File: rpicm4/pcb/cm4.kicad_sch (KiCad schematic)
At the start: 11 parts, among them J1 USB_C_Receptacle_USB2.0, J2 USB_C_Receptacle_USB2.0, J3 Conn_01x02_Male, J4 Conn_01x02_Male, J5 Conn_01x02_Male, J6 Conn_01x02_Male

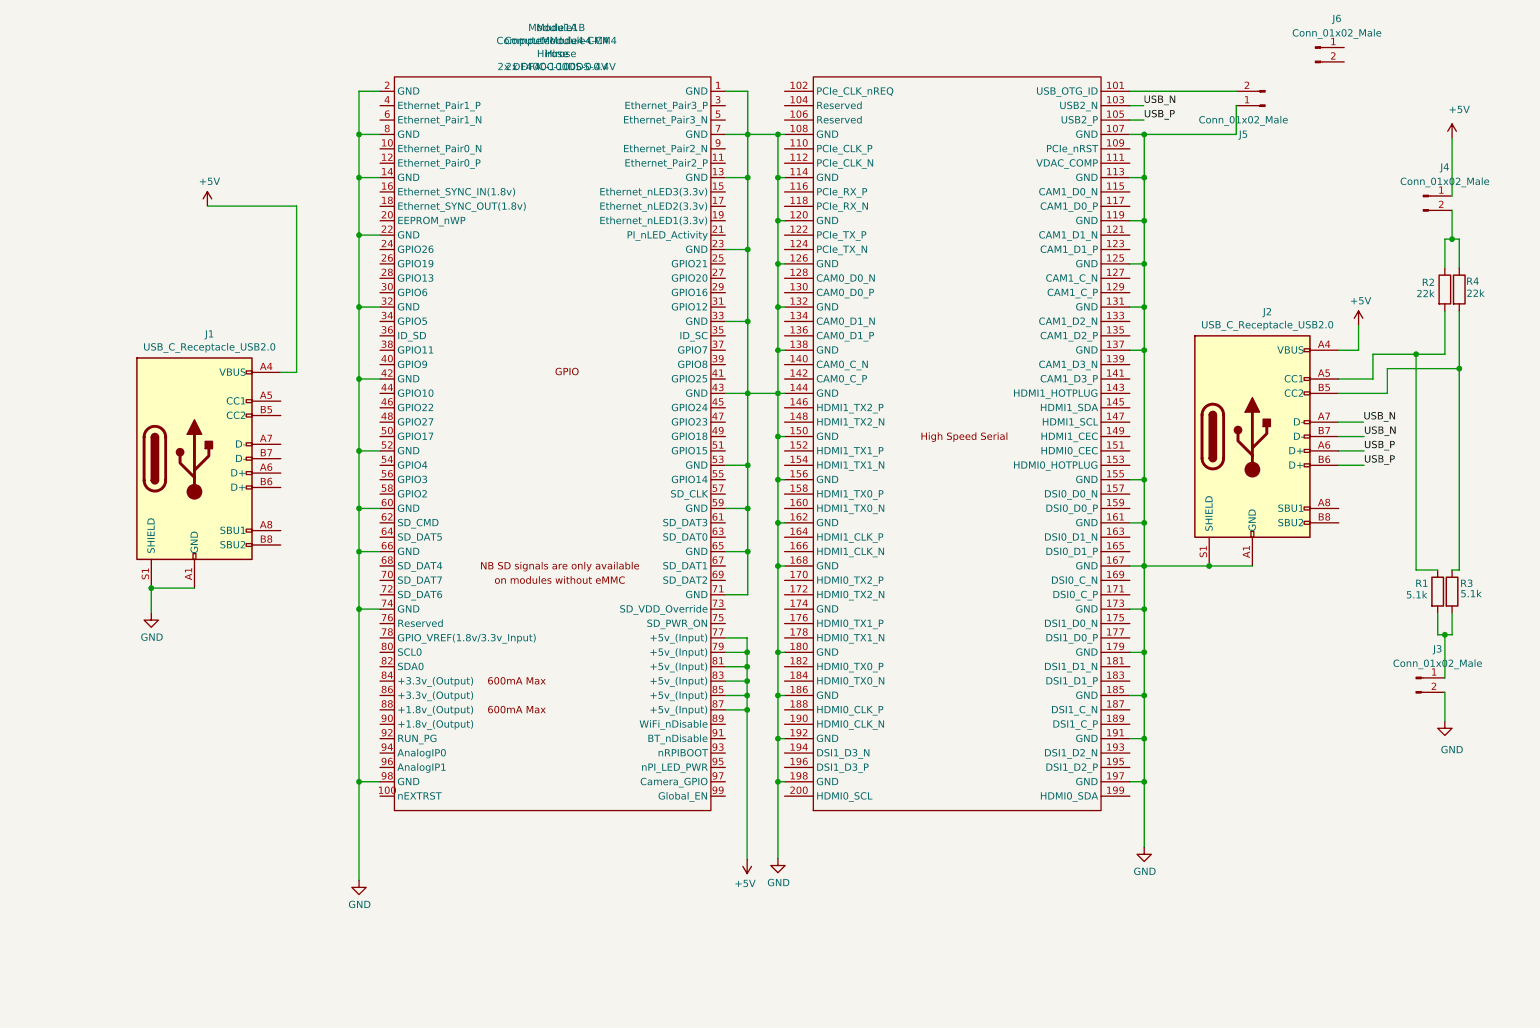
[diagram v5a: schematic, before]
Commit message: rpicm4: nRPIBOOT, UART, typec.cc
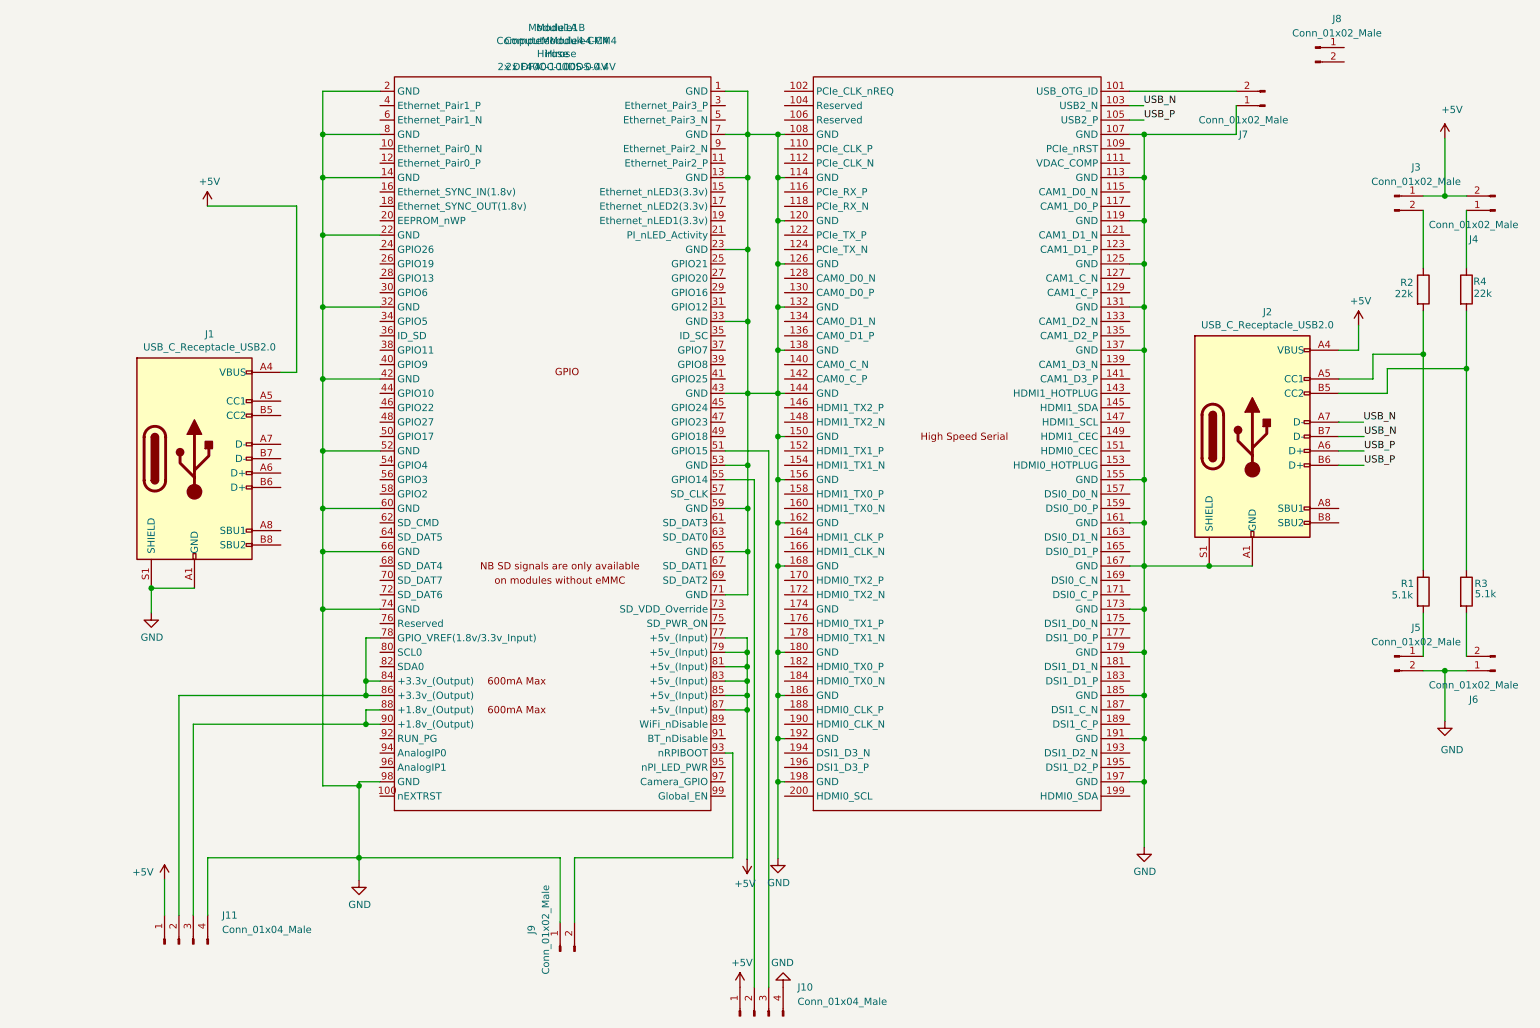
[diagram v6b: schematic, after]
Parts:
- added J10, J11: Conn_01x04_Male, Connector_PinHeader_2.54mm:PinHeader_1x04_P2.54mm_Vertical, symbol Connector:Conn_01x04_Male
- added J4, J6, J9: Conn_01x02_Male, Connector_PinHeader_2.54mm:PinHeader_1x02_P2.54mm_Vertical, symbol Connector:Conn_01x02_Male
- renumbered J4 to J3, J3 to J5, J5 to J7, J6 to J8
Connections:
- net +5V: now also J10.1 (Pin_1), J11.1 (Pin_1), J4.2 (Pin_2)
- net GND: now also J10.4 (Pin_4), J11.4 (Pin_4), J6.1 (Pin_1), J9.1 (Pin_1)
- net at J5.1 (Pin_1), R1.2: no longer R3.2
- net at J3.2 (Pin_2), R2.1: no longer R4.1
- net at Module1.51 (GPIO15): now also J10.3 (Pin_3)
- net at Module1.55 (GPIO14): now also J10.2 (Pin_2)
- net at Module1.78 (GPIO_VREF(1.8v/3.3v_Input)): now also Module1.84 (+3.3v_(Output)), Module1.86 (+3.3v_(Output)), J11.2 (Pin_2)
- net at Module1.88 (+1.8v_(Output)): now also Module1.90 (+1.8v_(Output)), J11.3 (Pin_3)
- net at Module1.93 (nRPIBOOT): now also J9.2 (Pin_2)
- new net: J6.2 (Pin_2), R3.2
- new net: J4.1 (Pin_1), R4.1
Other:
- moved on the sheet: J3, J5, R1, R2, R3, R4

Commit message: rpicm4: led pwr/act,analog 0/1,pwm 0/1,uart tx/rx
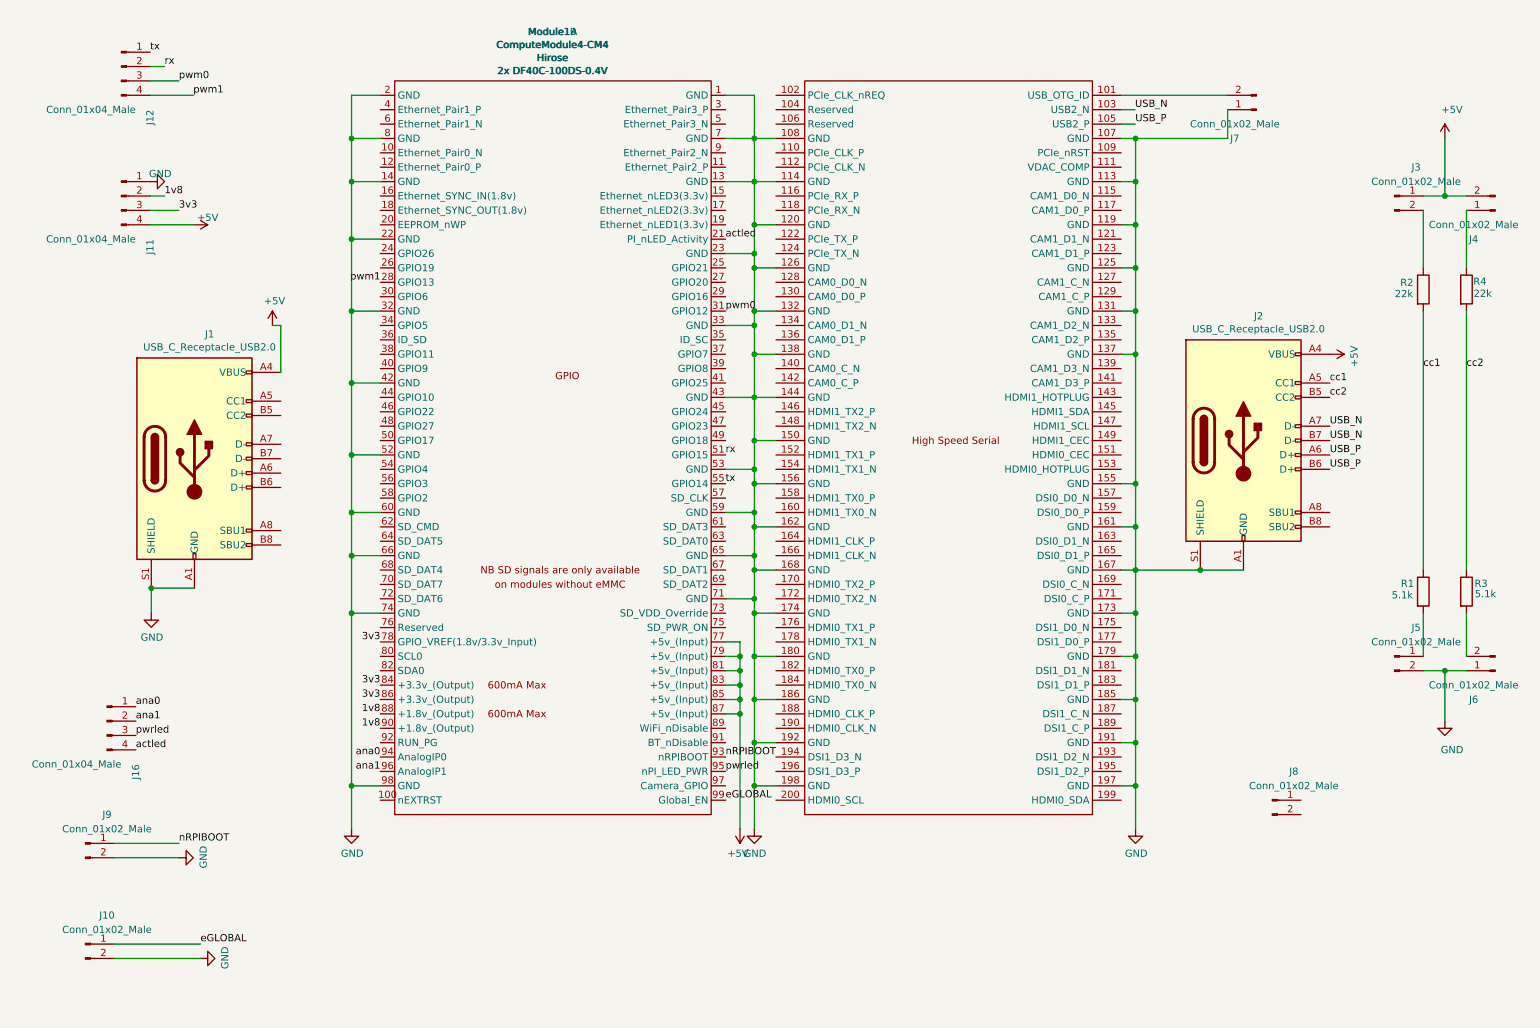
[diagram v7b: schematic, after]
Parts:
- removed J10: Conn_01x04_Male, Connector_PinHeader_2.54mm:PinHeader_1x04_P2.54mm_Vertical, symbol Connector:Conn_01x04_Male
- added J10: Conn_01x02_Male, Connector_PinHeader_2.54mm:PinHeader_1x02_P2.54mm_Vertical, symbol Connector:Conn_01x02_Male
- added J12, J16: Conn_01x04_Male, Connector_PinHeader_2.54mm:PinHeader_1x04_P2.54mm_Vertical, symbol Connector:Conn_01x04_Male
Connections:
- net +5V: now also J11.4 (Pin_4); no longer J11.1 (Pin_1)
- net GND: now also J11.1 (Pin_1), J9.2 (Pin_2), Module1.174 (GND), J10.2 (Pin_2); no longer J11.4 (Pin_4), J9.1 (Pin_1)
- net cc2: now reaches J2.B5 (CC2), R3.1, R4.2
- net cc1: now reaches J2.A5 (CC1), R1.1, R2.2
- net actled: now reaches Module1.21 (PI_nLED_Activity)
- net actled: now also J16.4 (Pin_4)
- net pwm1: now reaches Module1.28 (GPIO13)
- net pwm1: now also J12.4 (Pin_4)
- net pwm0: now reaches Module1.31 (GPIO12)
- net pwm0: now also J12.3 (Pin_3)
- net rx: now reaches Module1.51 (GPIO15)
- net rx: now also J12.2 (Pin_2)
- net tx: now reaches Module1.55 (GPIO14)
- net tx: now also J12.1 (Pin_1)
- net 3v3: now reaches Module1.78 (GPIO_VREF(1.8v/3.3v_Input)), Module1.84 (+3.3v_(Output)), Module1.86 (+3.3v_(Output))
- net 3v3: now also J11.3 (Pin_3); no longer J11.2 (Pin_2)
- net 1v8: now reaches Module1.88 (+1.8v_(Output)), Module1.90 (+1.8v_(Output))
- net 1v8: now also J11.2 (Pin_2); no longer J11.3 (Pin_3)
- net nRPIBOOT: now reaches Module1.93 (nRPIBOOT)
- net nRPIBOOT: now also J9.1 (Pin_1); no longer J9.2 (Pin_2)
- net ana0: now reaches Module1.94 (AnalogIP0)
- net ana0: now also J16.1 (Pin_1)
- net pwrled: now reaches Module1.95 (nPI_LED_PWR)
- net pwrled: now also J16.3 (Pin_3)
- net ana1: now reaches Module1.96 (AnalogIP1)
- net ana1: now also J16.2 (Pin_2)
- net eGLOBAL: now reaches Module1.99 (Global_EN)
- net eGLOBAL: now also J10.1 (Pin_1)
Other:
- moved on the sheet: J2, J7, J8, Module1A, Module1B

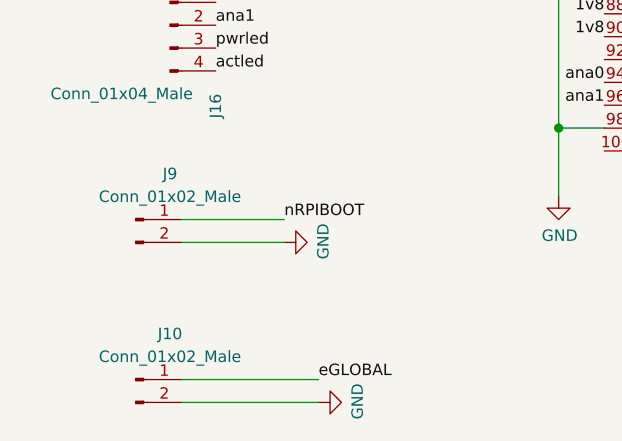
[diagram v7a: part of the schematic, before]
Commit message: rpicm4: round corner, better layout
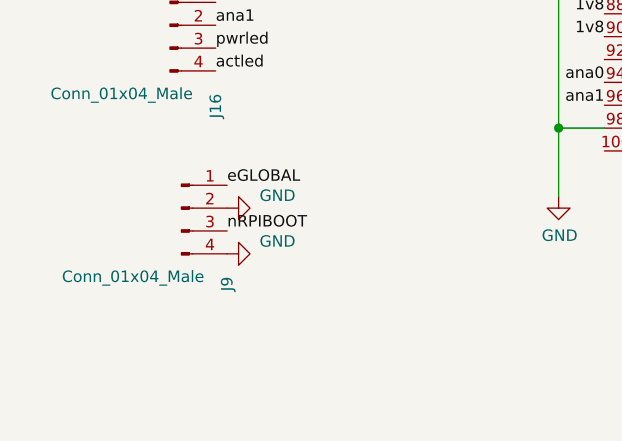
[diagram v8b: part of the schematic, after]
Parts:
- removed J10, J9: Conn_01x02_Male, Connector_PinHeader_2.54mm:PinHeader_1x02_P2.54mm_Vertical, symbol Connector:Conn_01x02_Male
- added J9: Conn_01x04_Male, Connector_PinHeader_2.54mm:PinHeader_1x04_P2.54mm_Vertical, symbol Connector:Conn_01x04_Male
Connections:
- net GND: now also J9.2 (Pin_2), J9.4 (Pin_4)
- net eGLOBAL: now also J9.1 (Pin_1)
- net nRPIBOOT: now also J9.3 (Pin_3)
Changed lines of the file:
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@@
   (junction (at 265.43 46.99) (diameter 1.016) (color 0 0 0 0))
   (junction (at 265.43 130.81) (diameter 1.016) (color 0 0 0 0))
-  (wire (pts (xy 30.48 161.29) (xy 41.91 161.29))
-    (stroke (width 0) (type solid) (color 0 0 0 0))
-  )
-  (wire (pts (xy 30.48 179.07) (xy 45.72 179.07))
-    (stroke (width 0) (type solid) (color 0 0 0 0))
-  )
   (wire (pts (xy 36.83 46.99) (xy 39.37 46.99))
     (stroke (width 0) (type solid) (color 0 0 0 0))
@@
     (stroke (width 0) (type solid) (color 0 0 0 0))
   )
-  (wire (pts (xy 41.91 163.83) (xy 30.48 163.83))
-    (stroke (width 0) (type solid) (color 0 0 0 0))
-  )
   (wire (pts (xy 44.45 29.21) (xy 36.83 29.21))
     (stroke (width 0) (type solid) (color 0 0 0 0))
   )
-  (wire (pts (xy 45.72 181.61) (xy 30.48 181.61))
-    (stroke (width 0) (type solid) (color 0 0 0 0))
-  )
   (wire (pts (xy 58.42 69.85) (xy 59.8932 69.85))
     (stroke (width 0) (type solid) (color 0 0 0 0))
@@
     (effects (font (size 1.27 1.27)) (justify left bottom))
   )
+  (label "eGLOBAL" (at 35.56 157.48 0)
+    (effects (font (size 1.27 1.27)) (justify left bottom))
+  )
+  (label "nRPIBOOT" (at 35.56 162.56 0)
+    (effects (font (size 1.27 1.27)) (justify left bottom))
+  )
   (label "tx" (at 36.83 21.59 0)
     (effects (font (size 1.27 1.27)) (justify left bottom))
@@
     (effects (font (size 1.27 1.27)) (justify left bottom))
   )
-  (label "nRPIBOOT" (at 41.91 161.29 0)
-    (effects (font (size 1.27 1.27)) (justify left bottom))
-  )
   (label "pwm1" (at 44.45 29.21 0)
-    (effects (font (size 1.27 1.27)) (justify left bottom))
-  )
-  (label "eGLOBAL" (at 45.72 179.07 0)
     (effects (font (size 1.27 1.27)) (justify left bottom))
   )
@@
     )
   )
+  (symbol (lib_id "power:GND") (at 35.56 160.02 90) (unit 1)
+    (in_bom yes) (on_board yes)
+    (property "Reference" "#PWR010" (id 0) (at 41.91 160.02 0)
+      (effects (font (size 1.27 1.27)) hide)
+    )
+    (property "Value" "GND" (id 1) (at 41.1544 158.6357 90))
+    (property "Footprint" "" (id 2) (at 35.56 160.02 0)
+      (effects (font (size 1.27 1.27)) hide)
+    )
+    (property "Datasheet" "" (id 3) (at 35.56 160.02 0)
+      (effects (font (size 1.27 1.27)) hide)
+    )
+  )
+  (symbol (lib_id "power:GND") (at 35.56 165.1 90) (unit 1)
+    (in_bom yes) (on_board yes)
+    (property "Reference" "#PWR012" (id 0) (at 41.91 165.1 0)
+      (effects (font (size 1.27 1.27)) hide)
+    )
+    (property "Value" "GND" (id 1) (at 41.1544 163.7157 90))
+    (property "Footprint" "" (id 2) (at 35.56 165.1 0)
+      (effects (font (size 1.27 1.27)) hide)
+    )
+    (property "Datasheet" "" (id 3) (at 35.56 165.1 0)
+      (effects (font (size 1.27 1.27)) hide)
+    )
+  )
   (symbol (lib_id "power:GND") (at 36.83 44.45 90) (unit 1)
     (in_bom yes) (on_board yes)
@@
     )
   )
-  (symbol (lib_id "power:GND") (at 41.91 163.83 90) (unit 1)
-    (in_bom yes) (on_board yes)
-    (property "Reference" "#PWR010" (id 0) (at 48.26 163.83 0)
-      (effects (font (size 1.27 1.27)) hide)
-    )
-    (property "Value" "GND" (id 1) (at 46.2344 163.7157 0))
-    (property "Footprint" "" (id 2) (at 41.91 163.83 0)
-      (effects (font (size 1.27 1.27)) hide)
-    )
-    (property "Datasheet" "" (id 3) (at 41.91 163.83 0)
-      (effects (font (size 1.27 1.27)) hide)
-    )
-  )
-  (symbol (lib_id "power:GND") (at 45.72 181.61 90) (unit 1)
-    (in_bom yes) (on_board yes)
-    (property "Reference" "#PWR012" (id 0) (at 52.07 181.61 0)
-      (effects (font (size 1.27 1.27)) hide)
-    )
-    (property "Value" "GND" (id 1) (at 50.0444 181.4957 0))
-    (property "Footprint" "" (id 2) (at 45.72 181.61 0)
-      (effects (font (size 1.27 1.27)) hide)
-    )
-    (property "Datasheet" "" (id 3) (at 45.72 181.61 0)
-      (effects (font (size 1.27 1.27)) hide)
-    )
-  )
   (symbol (lib_id "power:GND") (at 72.39 158.75 0) (unit 1)
     (in_bom yes) (on_board yes)
@@
     )
     (property "Datasheet" "~" (id 3) (at 269.24 116.84 0)
-      (effects (font (size 1.27 1.27)) hide)
-    )
-  )
-  (symbol (lib_id "Connector:Conn_01x02_Male") (at 25.4 161.29 0) (unit 1)
-    (in_bom yes) (on_board yes)
-    (property "Reference" "J9" (id 0) (at 29.21 156.21 0))
-    (property "Value" "Conn_01x02_Male" (id 1) (at 29.21 158.75 0))
-    (property "Footprint" "Connector_PinHeader_2.54mm:PinHeader_1x02_P2.54mm_Vertical" (id 2) (at 25.4 161.29 0)
-      (effects (font (size 1.27 1.27)) hide)
-    )
-    (property "Datasheet" "~" (id 3) (at 25.4 161.29 0)
-      (effects (font (size 1.27 1.27)) hide)
-    )
-  )
-  (symbol (lib_id "Connector:Conn_01x02_Male") (at 25.4 179.07 0) (unit 1)
-    (in_bom yes) (on_board yes)
-    (property "Reference" "J10" (id 0) (at 29.21 173.99 0))
-    (property "Value" "Conn_01x02_Male" (id 1) (at 29.21 176.53 0))
-    (property "Footprint" "Connector_PinHeader_2.54mm:PinHeader_1x02_P2.54mm_Vertical" (id 2) (at 25.4 179.07 0)
-      (effects (font (size 1.27 1.27)) hide)
-    )
-    (property "Datasheet" "~" (id 3) (at 25.4 179.07 0)
       (effects (font (size 1.27 1.27)) hide)
     )
@@
     )
   )
+  (symbol (lib_id "Connector:Conn_01x04_Male") (at 30.48 160.02 0) (unit 1)
+    (in_bom yes) (on_board yes)
+    (property "Reference" "J9" (id 0) (at 35.56 167.64 90)
+      (effects (font (size 1.27 1.27)) (justify right))
+    )
+    (property "Value" "Conn_01x04_Male" (id 1) (at 33.02 167.64 0)
+      (effects (font (size 1.27 1.27)) (justify right))
+    )
+    (property "Footprint" "Connector_PinHeader_2.54mm:PinHeader_1x04_P2.54mm_Vertical" (id 2) (at 30.48 160.02 0)
+      (effects (font (size 1.27 1.27)) hide)
+    )
+    (property "Datasheet" "~" (id 3) (at 30.48 160.02 0)
+      (effects (font (size 1.27 1.27)) hide)
+    )
+  )
   (symbol (lib_id "Connector:Conn_01x04_Male") (at 31.75 24.13 0) (unit 1)
     (in_bom yes) (on_board yes)
@@
       (reference "J8") (unit 1) (value "Conn_01x02_Male") (footprint "Connector_PinHeader_2.54mm:PinHeader_1x02_P2.54mm_Vertical")
     )
-    (path "/5eabf67d-0efd-4178-a31d-be78b7f9e105"
-      (reference "J9") (unit 1) (value "Conn_01x02_Male") (footprint "Connector_PinHeader_2.54mm:PinHeader_1x02_P2.54mm_Vertical")
-    )
-    (path "/c46ac9ba-22ae-4098-a0a0-b7cd170bc856"
-      (reference "J10") (unit 1) (value "Conn_01x02_Male") (footprint "Connector_PinHeader_2.54mm:PinHeader_1x02_P2.54mm_Vertical")
+    (path "/e604befe-3fa9-4661-a885-1c1db25e4f74"
+      (reference "J9") (unit 1) (value "Conn_01x04_Male") (footprint "Connector_PinHeader_2.54mm:PinHeader_1x04_P2.54mm_Vertical")
     )
     (path "/a87c1880-0fa3-4829-b9a7-778f6121f596"
